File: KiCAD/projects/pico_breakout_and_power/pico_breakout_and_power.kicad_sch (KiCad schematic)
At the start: 3 parts, among them J1 Conn_01x17_Socket, J12 Conn_01x17_Socket

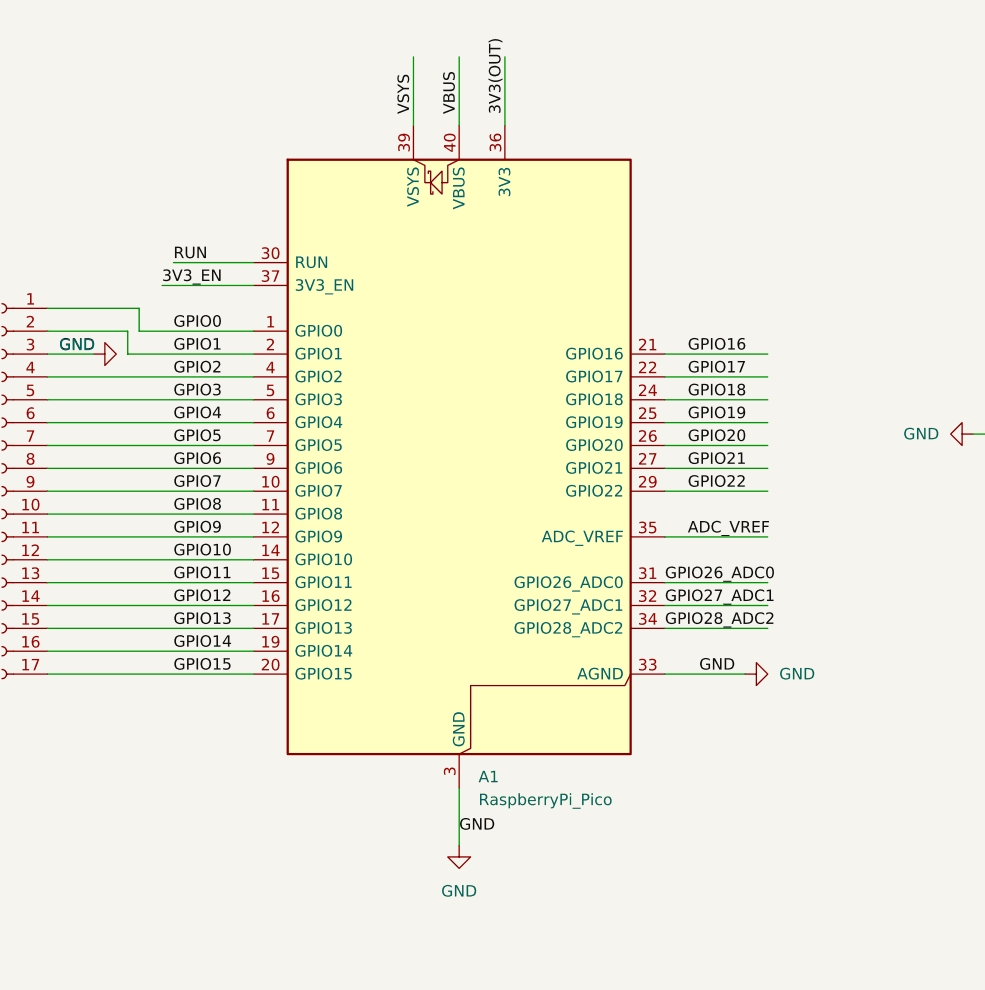
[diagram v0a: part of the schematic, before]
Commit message: Made grouped 3d model of pico with sockets
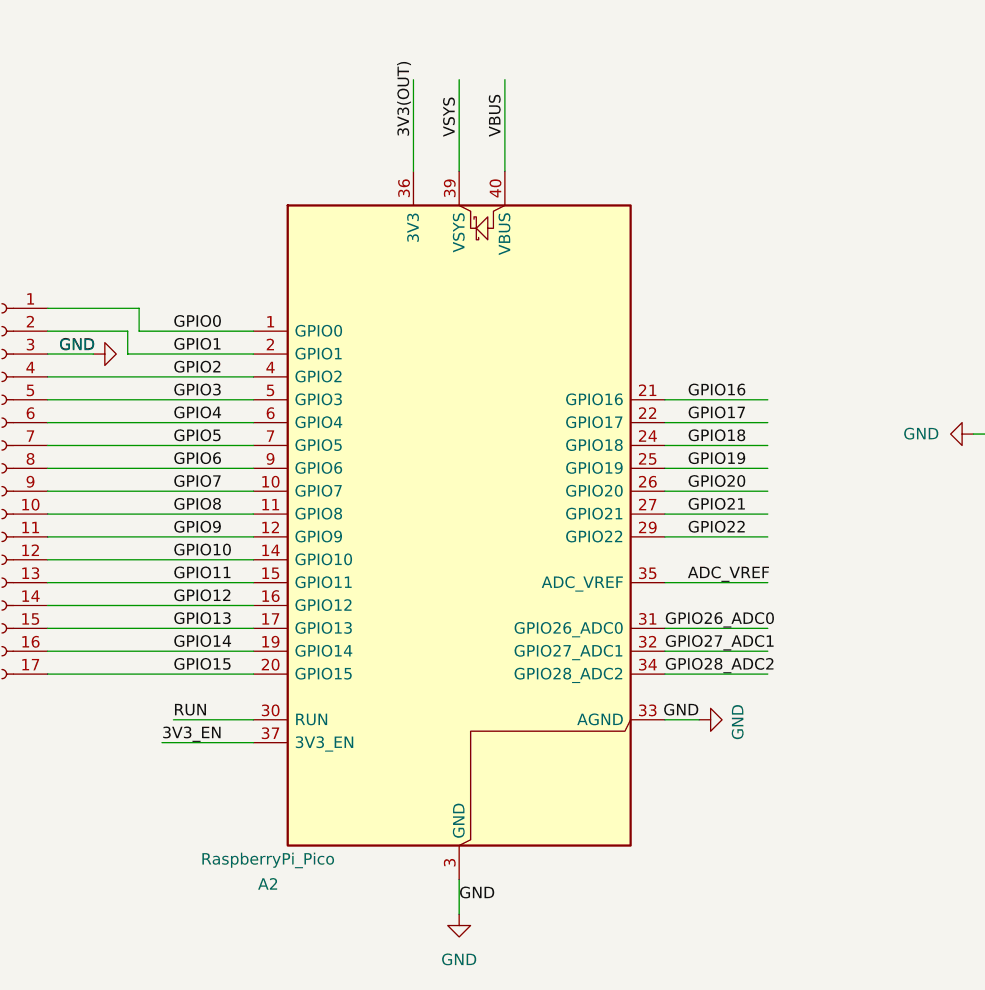
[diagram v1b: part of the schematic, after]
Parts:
- removed A1: RaspberryPi_Pico, Module:RaspberryPi_Pico_SMD, symbol MCU_Module:RaspberryPi_Pico
- added A2: RaspberryPi_Pico, Module_RaspberryPi_Pico:RaspberryPi_Pico_Common_THT, symbol MCU_Module_RaspberryPi_Pico:RaspberryPi_Pico
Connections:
- net 3V3(OUT): now also A2.36 (3V3)
- net 3V3_EN: now also A2.37 (3V3_EN)
- net ADC_VREF: now also A2.35 (ADC_VREF)
- net GND: now also A2.13 (GND), A2.18 (GND), A2.23 (GND), A2.28 (GND), A2.3 (GND), A2.33 (AGND), A2.38 (GND), A2.8 (GND)
- net GPIO0: now also A2.1 (GPIO0)
- net GPIO1: now also A2.2 (GPIO1)
- net GPIO10: now also A2.14 (GPIO10)
- net GPIO11: now also A2.15 (GPIO11)
- net GPIO12: now also A2.16 (GPIO12)
- net GPIO13: now also A2.17 (GPIO13)
- net GPIO14: now also A2.19 (GPIO14)
- net GPIO15: now also A2.20 (GPIO15)
- net GPIO16: now also A2.21 (GPIO16)
- net GPIO17: now also A2.22 (GPIO17)
- net GPIO18: now also A2.24 (GPIO18)
- net GPIO19: now also A2.25 (GPIO19)
- net GPIO2: now also A2.4 (GPIO2)
- net GPIO20: now also A2.26 (GPIO20)
- net GPIO21: now also A2.27 (GPIO21)
- net GPIO22: now also A2.29 (GPIO22)
- net GPIO26_ADC0: now also A2.31 (GPIO26_ADC0)
- net GPIO27_ADC1: now also A2.32 (GPIO27_ADC1)
- net GPIO28_ADC2: now also A2.34 (GPIO28_ADC2)
- net GPIO3: now also A2.5 (GPIO3)
- net GPIO4: now also A2.6 (GPIO4)
- net GPIO5: now also A2.7 (GPIO5)
- net GPIO6: now also A2.9 (GPIO6)
- net GPIO7: now also A2.10 (GPIO7)
- net GPIO8: now also A2.11 (GPIO8)
- net GPIO9: now also A2.12 (GPIO9)
- net RUN: now also A2.30 (RUN)
- net VBUS: now also A2.40 (VBUS)
- net VSYS: now also A2.39 (VSYS)

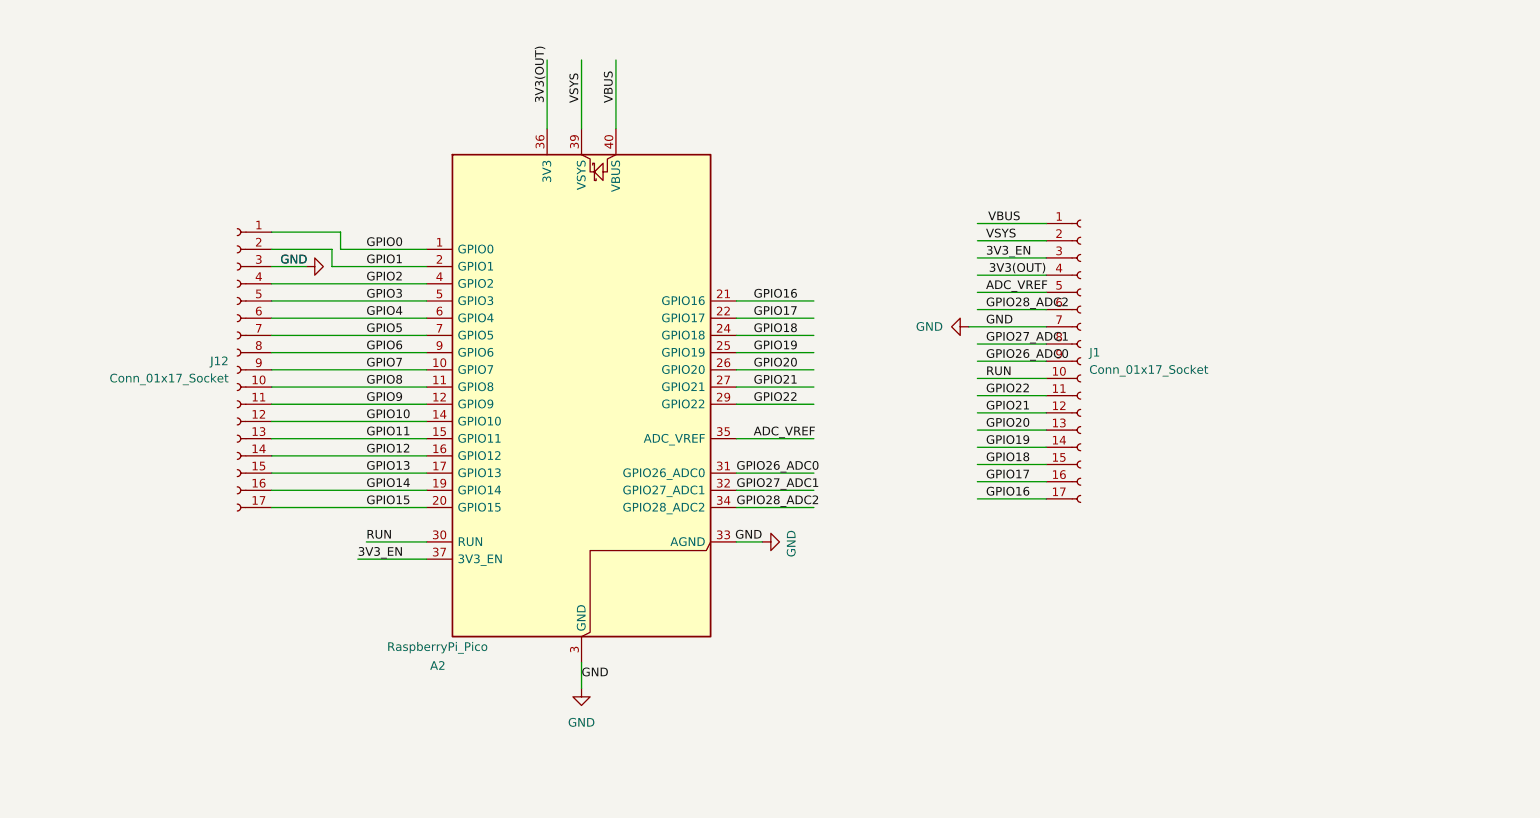
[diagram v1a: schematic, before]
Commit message: Combining pico and LED driver circuits
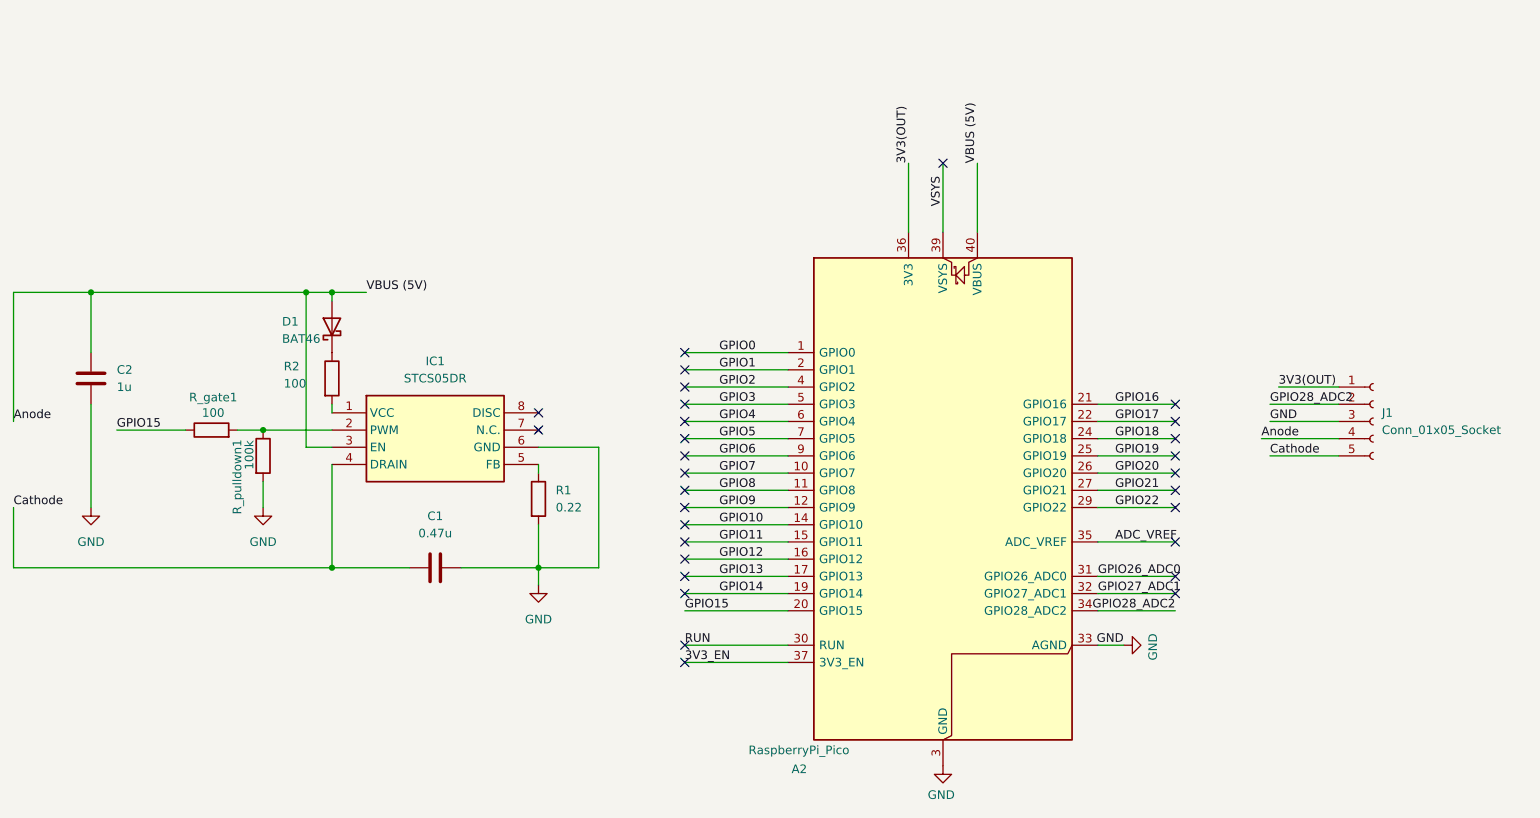
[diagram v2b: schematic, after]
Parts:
- removed J1, J12: Conn_01x17_Socket, Connector_PinSocket_2.54mm:PinSocket_1x17_P2.54mm_Vertical, symbol Connector:Conn_01x17_Socket
- added C1: 0.47u, Capacitor_THT:C_Disc_D10.5mm_W5.0mm_P10.00mm, symbol Device:C
- added C2: 1u, Capacitor_THT:C_Disc_D10.5mm_W5.0mm_P10.00mm, symbol Device:C
- added D1: BAT46, Diode_THT:D_DO-35_SOD27_P7.62mm_Horizontal, symbol Diode:BAT46
- added IC1: STCS05DR, Aidan_DST_footprints:SOIC127P600X175-8N, symbol STCS05DR:STCS05DR
- added J1: Conn_01x05_Socket, Connector_JST:JST_EH_S5B-EH_1x05_P2.50mm_Horizontal, symbol Connector:Conn_01x05_Socket
- added R1: 0.22, Resistor_THT:R_Axial_DIN0411_L9.9mm_D3.6mm_P12.70mm_Horizontal, symbol Device:R
- added R2, R_gate1: 100, Resistor_THT:R_Axial_DIN0207_L6.3mm_D2.5mm_P10.16mm_Horizontal, symbol Device:R
- added R_pulldown1: 100k, Resistor_THT:R_Axial_DIN0207_L6.3mm_D2.5mm_P10.16mm_Horizontal, symbol Device:R
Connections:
- net 3V3(OUT): now also J1.1 (Pin_1)
- net GND: now also C1.2, C2.2, IC1.6 (GND), J1.3 (Pin_3), R1.2, R_pulldown1.2
- net GPIO15: now also R_gate1.1
- net GPIO28_ADC2: now also J1.2 (Pin_2)
- net VBUS renamed Anode
- net Anode: now also C2.1, D1.2 (A), IC1.3 (EN), J1.4 (Pin_4)
- new net: D1.1 (K), R2.1
- new net: IC1.2 (PWM), R_gate1.2, R_pulldown1.1
- new net: IC1.1 (VCC), R2.2
- new net: IC1.5 (FB), R1.1
- new net Cathode: C1.1, IC1.4 (DRAIN), J1.5 (Pin_5)
- no-connect marks 0 -> 30
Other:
- moved on the sheet: A2

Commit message: Routed combined pico board
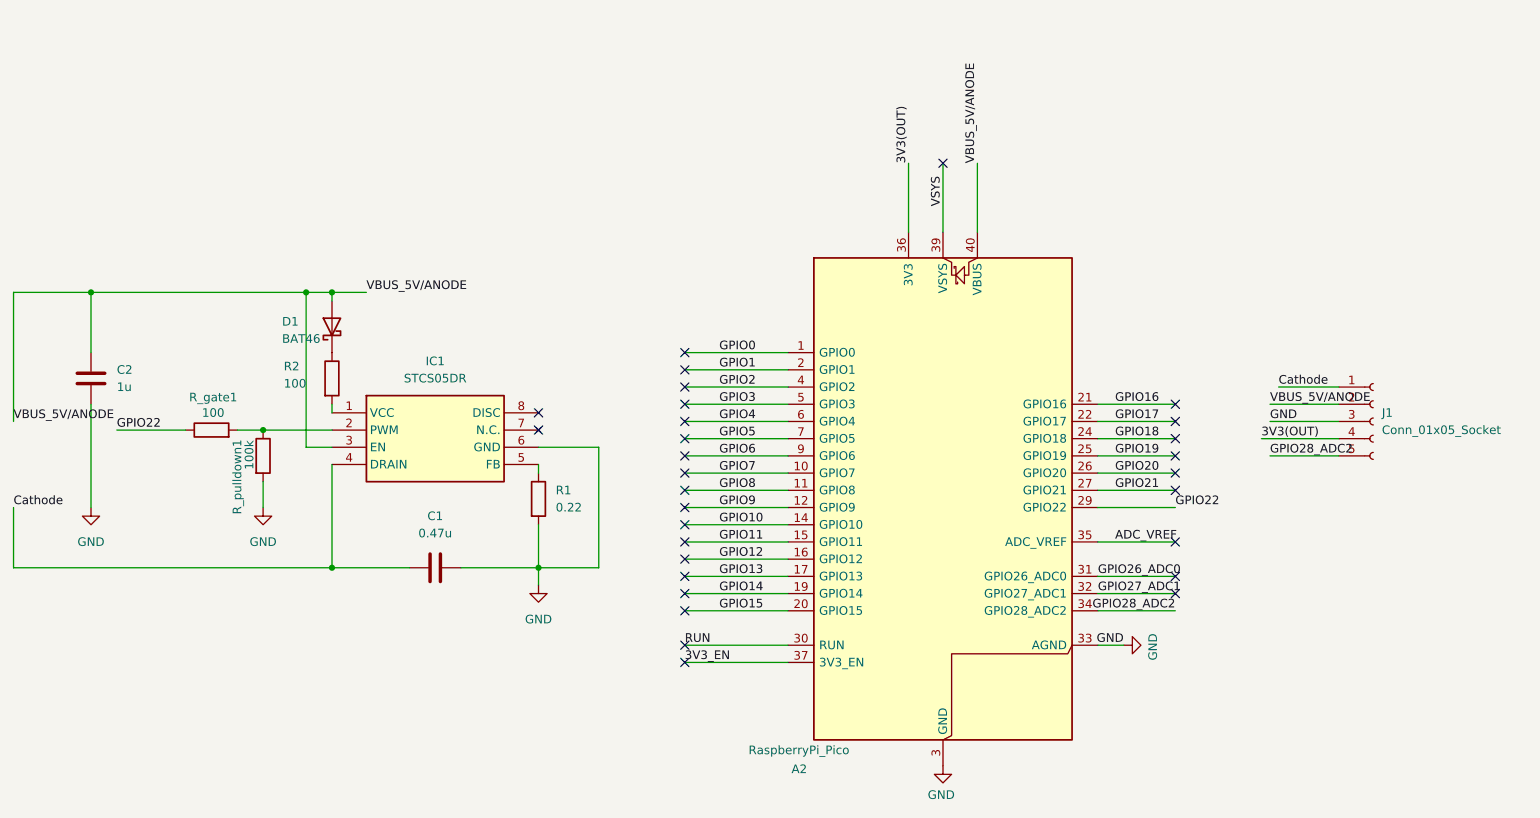
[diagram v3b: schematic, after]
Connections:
- net 3V3(OUT): now also J1.4 (Pin_4); no longer J1.1 (Pin_1)
- net Cathode: now also J1.1 (Pin_1); no longer J1.5 (Pin_5)
- net GPIO15: no longer R_gate1.1
- net GPIO22: now also R_gate1.1
- net GPIO28_ADC2: now also J1.5 (Pin_5); no longer J1.2 (Pin_2)
- net Anode renamed VBUS_5V/ANODE
- net VBUS_5V/ANODE: now also J1.2 (Pin_2); no longer J1.4 (Pin_4)
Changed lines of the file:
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@@
+	)
+	(no_connect
+		(at 158.75 130.81)
 	)
 	(no_connect
@@
 	)
 	(no_connect
-		(at 231.14 115.57)
-	)
-	(no_connect
 		(at 158.75 120.65)
 	)
@@
 	(wire
 		(pts
+			(xy 219.71 115.57) (xy 231.14 115.57)
+		)
+		(stroke
+			(width 0)
+			(type default)
+		)
+	)
+	(wire
+		(pts
 			(xy 137.16 106.68) (xy 146.05 106.68)
 		)
@@
 	(wire
 		(pts
+			(xy 158.75 130.81) (xy 173.99 130.81)
+		)
+		(stroke
+			(width 0)
+			(type default)
+		)
+	)
+	(wire
+		(pts
 			(xy 106.68 100.33) (xy 106.68 101.6)
 		)
@@
 	(wire
 		(pts
-			(xy 231.14 115.57) (xy 219.71 115.57)
-		)
-		(stroke
-			(width 0)
-			(type default)
-		)
-	)
-	(wire
-		(pts
 			(xy 231.14 113.03) (xy 219.71 113.03)
 		)
@@
 	(wire
 		(pts
-			(xy 158.75 130.81) (xy 173.99 130.81)
-		)
-		(stroke
-			(width 0)
-			(type default)
-		)
-	)
-	(wire
-		(pts
 			(xy 231.14 130.81) (xy 219.71 130.81)
 		)
@@
 			(width 0)
 			(type default)
+		)
+	)
+	(label "3V3(OUT)"
+		(at 243.84 105.41 0)
+		(effects
+			(font
+				(size 1.27 1.27)
+			)
+			(justify left bottom)
+		)
+	)
+	(label "VBUS_5V{slash}ANODE"
+		(at 59.69 102.87 0)
+		(effects
+			(font
+				(size 1.27 1.27)
+			)
+			(justify left bottom)
 		)
 	)
@@
 		)
 	)
-	(label "VBUS (5V)"
+	(label "VBUS_5V{slash}ANODE"
 		(at 111.76 83.82 0)
 		(effects
@@
 		)
 	)
+	(label "GPIO28_ADC2"
+		(at 245.11 107.95 0)
+		(effects
+			(font
+				(size 1.27 1.27)
+			)
+			(justify left bottom)
+		)
+	)
 	(label "GPIO7"
 		(at 163.83 110.49 0)
@@
 		)
 	)
-	(label "Anode"
-		(at 59.69 102.87 0)
-		(effects
-			(font
-				(size 1.27 1.27)
-			)
-			(justify left bottom)
-		)
-	)
-	(label "3V3(OUT)"
-		(at 246.38 97.79 0)
-		(effects
-			(font
-				(size 1.27 1.27)
-			)
-			(justify left bottom)
-		)
-	)
 	(label "GPIO14"
 		(at 163.83 128.27 0)
@@
 	)
 	(label "GPIO15"
-		(at 158.75 130.81 0)
-		(effects
-			(font
-				(size 1.27 1.27)
-			)
-			(justify left bottom)
-		)
-	)
-	(label "Anode"
-		(at 243.84 105.41 0)
+		(at 163.83 130.81 0)
 		(effects
 			(font
@@
 		)
 	)
-	(label "Cathode"
-		(at 245.11 107.95 0)
-		(effects
-			(font
-				(size 1.27 1.27)
-			)
-			(justify left bottom)
-		)
-	)
 	(label "GPIO19"
 		(at 222.25 107.95 0)
@@
 		)
 	)
-	(label "VBUS (5V)"
+	(label "VBUS_5V{slash}ANODE"
 		(at 201.93 64.77 90)
 		(effects
@@
 		)
 	)
-	(label "GPIO28_ADC2"
-		(at 245.11 100.33 0)
+	(label "GPIO22"
+		(at 74.93 104.14 0)
 		(effects
 			(font
@@
 	)
 	(label "GPIO22"
-		(at 222.25 115.57 0)
+		(at 231.14 115.57 0)
 		(effects
 			(font
@@
 		)
 	)
+	(label "Cathode"
+		(at 246.38 97.79 0)
+		(effects
+			(font
+				(size 1.27 1.27)
+			)
+			(justify left bottom)
+		)
+	)
 	(label "GPIO16"
 		(at 222.25 100.33 0)
@@
 		)
 	)
-	(label "GPIO15"
-		(at 74.93 104.14 0)
-		(effects
-			(font
-				(size 1.27 1.27)
-			)
-			(justify left bottom)
-		)
-	)
 	(label "GPIO10"
 		(at 163.83 118.11 0)
 		(effects
 			(font
+				(size 1.27 1.27)
+			)
+			(justify left bottom)
+		)
+	)
+	(label "VBUS_5V{slash}ANODE"
+		(at 245.11 100.33 0)
+		(effects
+			(font
